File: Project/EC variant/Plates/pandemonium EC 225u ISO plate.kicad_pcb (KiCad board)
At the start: 2 copper layers, 199.9 x 81 mm, 36 parts

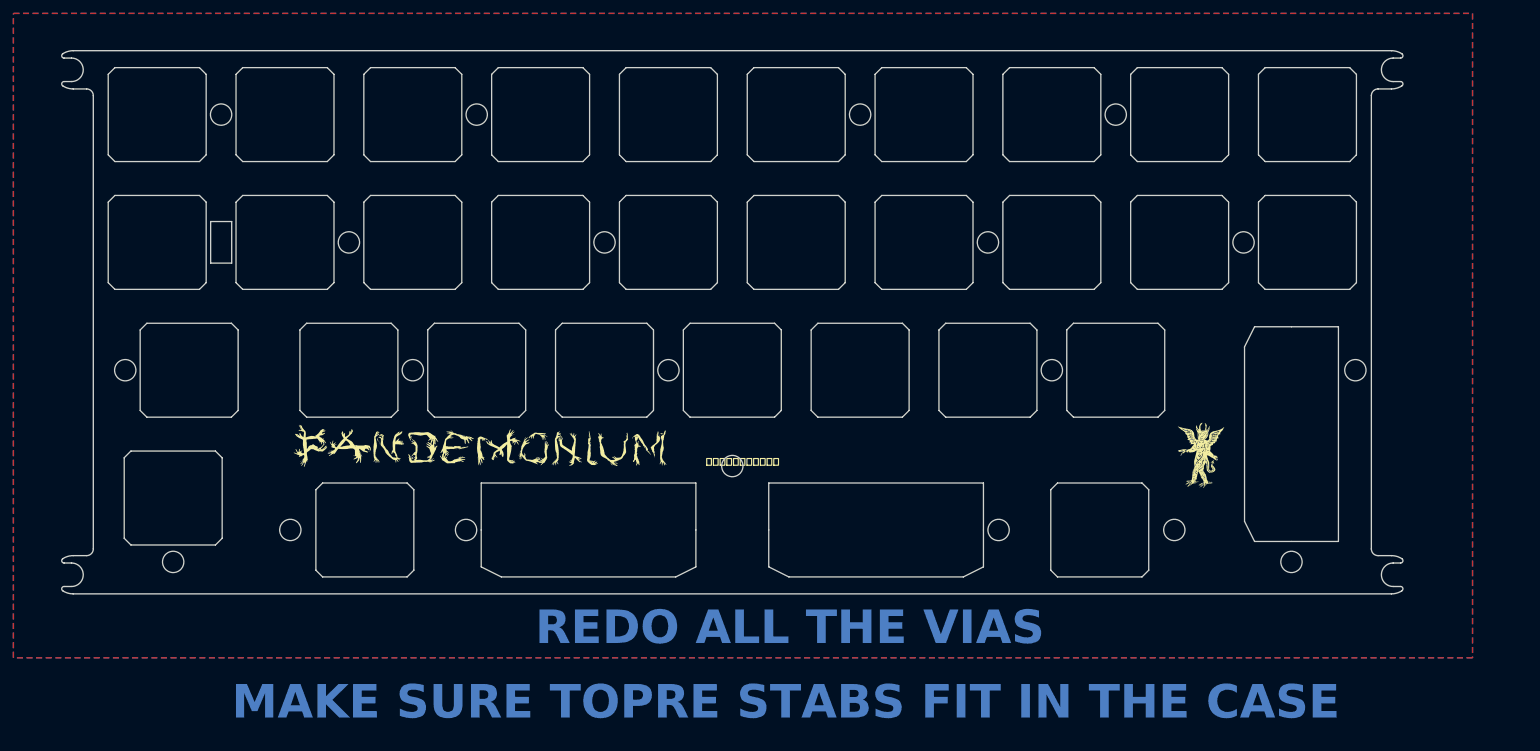
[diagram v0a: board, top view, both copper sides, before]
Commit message: changes to topre version and BLE version
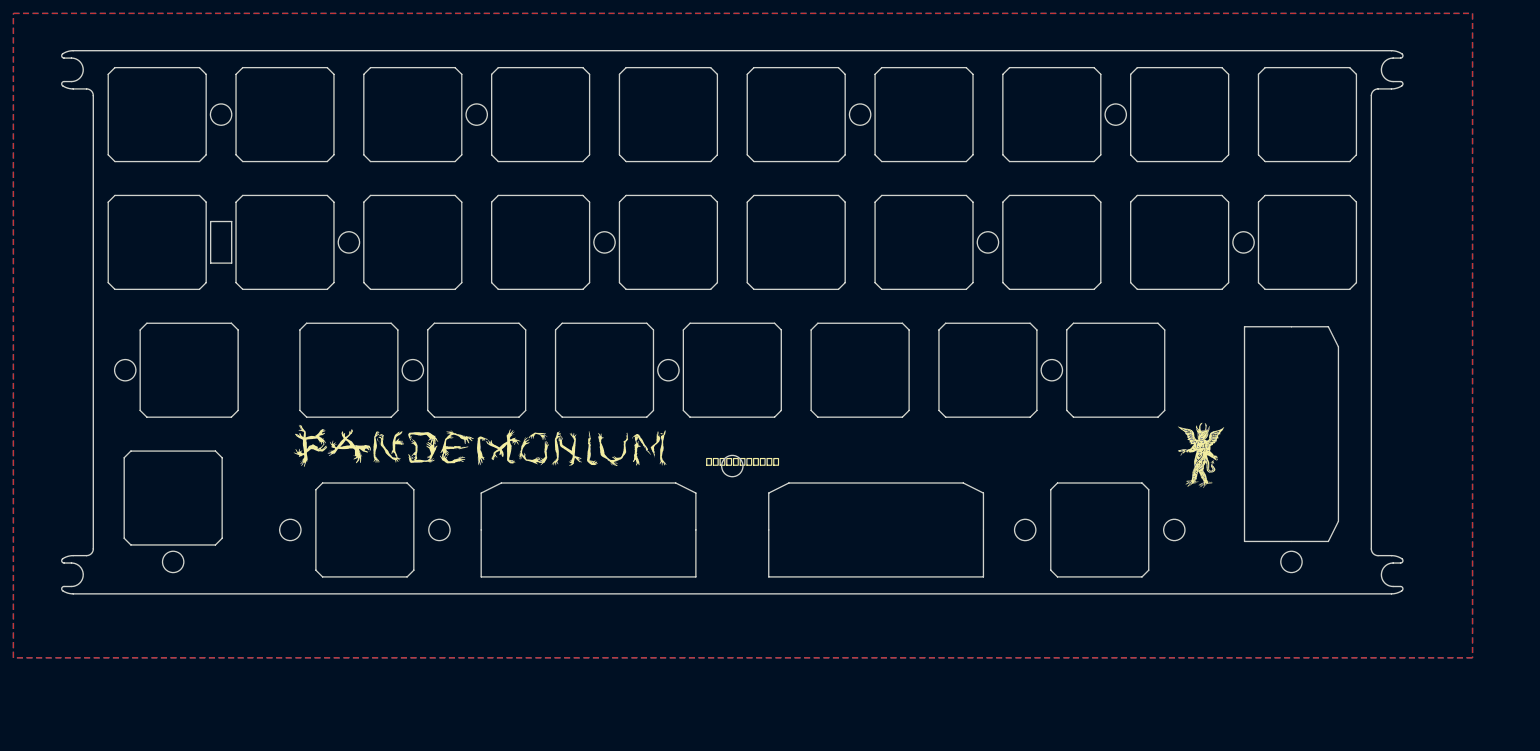
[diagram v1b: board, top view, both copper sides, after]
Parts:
- turned REF** to 180 degrees (x2)
- turned REF** to 90 degrees
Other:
- outline, holes or cut-outs redrawn
- board text removed: "MAKE SURE TOPRE STABS FIT IN THE CASE"
- board text removed: "REDO ALL THE VIAS"
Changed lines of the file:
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@@
   )
   (footprint "cipulot_parts:ecs_plate_cut_2U" (layer "F.Cu")
-    (at 148.43125 95.25)
+    (at 148.43125 95.25 180)
     (descr " StepUp generated footprint")
     (attr smd)
@@
   )
   (footprint "cipulot_parts:ecs_plate_cut_2U" (layer "F.Cu")
-    (at 210.34375 80.9625 -90)
+    (at 210.34375 80.9625 90)
     (descr " StepUp generated footprint")
     (attr smd)
@@
   )
   (footprint "cipulot_parts:ecs_plate_cut_2U" (layer "F.Cu")
-    (at 105.56875 95.25)
+    (at 105.56875 95.25 180)
     (descr " StepUp generated footprint")
     (attr smd)
@@
   (gr_line (start 28.500556 28.4125) (end 27.393534 28.4125)
     (stroke (width 0.2) (type solid)) (layer "Edge.Cuts"))
-  (gr_circle (center 219.86875 71.4375) (end 219.86875 69.85)
-    (stroke (width 0.1) (type default)) (fill none) (layer "Edge.Cuts"))
   (gr_arc (start 27.203629 29.0565) (mid 27.057812 28.663501) (end 27.393534 28.4125)
     (stroke (width 0.2) (type solid)) (layer "Edge.Cuts"))
@@
   (gr_arc (start 30.75 29.5125) (mid 31.457107 29.805393) (end 31.75 30.5125)
     (stroke (width 0.2) (type solid)) (layer "Edge.Cuts"))
-  (gr_circle (center 87.3125 95.25) (end 87.3125 93.6625)
+  (gr_circle (center 83.34375 95.25) (end 83.34375 93.6625)
     (stroke (width 0.1) (type default)) (fill none) (layer "Edge.Cuts"))
   (gr_line (start 226.606466 103.675) (end 225.499444 103.675)
@@
   (gr_arc (start 28.75 104.775) (mid 27.943898 104.658624) (end 27.203628 104.319)
     (stroke (width 0.2) (type solid)) (layer "Edge.Cuts"))
-  (gr_circle (center 166.6875 95.25) (end 166.6875 93.6625)
+  (gr_circle (center 170.65625 95.25) (end 170.65625 93.6625)
     (stroke (width 0.1) (type default)) (fill none) (layer "Edge.Cuts"))
   (gr_line (start 28.500555 103.675) (end 27.393534 103.675)
@@
   (gr_arc (start 27.203628 99.531) (mid 27.943898 99.191376) (end 28.75 99.075)
     (stroke (width 0.2) (type solid)) (layer "Edge.Cuts"))
-  (gr_text "REDO ALL THE VIAS" (at 97.63125 112.7125) (layer "B.Cu")
-    (effects (font (size 5 5) (thickness 0.3) bold) (justify left bottom))
-  )
-  (gr_text "MAKE SURE TOPRE STABS FIT IN THE CASE" (at 52.3875 123.825) (layer "B.Cu")
-    (effects (font (size 5 5) (thickness 0.3) bold) (justify left bottom))
-  )
   (gr_text "JLCJLCJLCJLC" (at 127 25.4) (layer "B.SilkS")
     (effects (font (size 1 1) (thickness 0.15)))
